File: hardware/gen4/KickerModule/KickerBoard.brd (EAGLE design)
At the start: 139.1 x 149.2 mm, 117 parts

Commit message: bit more work
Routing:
- net 3.3V: track 281.2 -> 507.0 mm, vias 8 -> 15
- net M1QB-3: track 0.00 -> 47.2 mm, vias 0 -> 1
- net SCK: track 106.7 -> 96.9 mm
- net MISO: track 98.2 -> 101.5 mm, vias 4 -> 6

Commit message: bit more work
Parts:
- added R22: 1k, SparkFun-Passives:0805
- added U$12: 13VZENER, rfc:THROUGH-HOLE-2
- moved PW_LED1 6.35 mm to (31.1, 94.6), flipped to the top, turned to 180 degrees
- moved CAP+_TEST 3.81 mm to (109.2, 134.0)
- moved R21 1.42 mm to (31.8, 89.5), turned to 270 degrees
- moved TMP 1.42 mm to (29.8, 89.5), turned to 90 degrees
- moved 3.3V_TEST 0.63 mm to (36.2, 94.6)
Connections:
- net 12V: now also U$12.-
- net 12VGND: now also U$12.+
- net 3.3V: now also R22.1
- net CHARGE_DONE: now also R22.2
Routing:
- net CHARGE_DONE: track 115.4 -> 150.0 mm
- net 12V: track 448.4 -> 475.8 mm
- net 3.3V: track 507.0 -> 523.8 mm, vias 15 -> 16
- net 12VGND: track 691.1 -> 700.0 mm
- net N$23: track 2.68 -> 11.0 mm, vias 0 -> 1
- net CAP+: track 190.0 -> 194.0 mm
- net GND: track 587.0 -> 585.0 mm

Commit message: new sizes + fixes
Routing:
- removed copper zone on layer 1, net 12VGND
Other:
- board size 139.1 x 149.2 mm -> 317.6 x 151.4 mm
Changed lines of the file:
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@@
 <setting verticaltext="up"/>
 </settings>
-<grid distance="0.635" unitdist="mm" unit="mil" style="lines" multiple="1" display="no" altdistance="0.3175" altunitdist="mm" altunit="mil"/>
+<grid distance="1" unitdist="mil" unit="mil" style="lines" multiple="1" display="no" altdistance="0.3175" altunitdist="mm" altunit="mil"/>
 <layers>
 <layer number="1" name="Top" color="4" fill="1" visible="yes" active="yes"/>
@@
 <wire x1="0" y1="20.955" x2="0" y2="119.365" width="0.4064" layer="20"/>
 <text x="-11.43" y="55.88" size="1.778" layer="20" rot="R90">MOTOR BOARD DIMENSION</text>
+<circle x="-156.54451875" y="29.649165625" radius="1.5875" width="0" layer="20"/>
+<circle x="-172.5444875" y="76.1492" radius="1.5875" width="0" layer="20"/>
+<circle x="-55.54471875" y="29.649165625" radius="1.5875" width="0" layer="20"/>
+<circle x="-156.54451875" y="128.149096875" radius="1.5875" width="0" layer="20"/>
+<circle x="-55.54471875" y="128.149096875" radius="1.5875" width="0" layer="20"/>
+<circle x="-39.544496875" y="76.1492" radius="1.5875" width="0" layer="20"/>
+<wire x1="-68.54469375" y1="7.649209375" x2="-33.544509375" y2="42.649140625" width="0" layer="20"/>
+<wire x1="-143.54454375" y1="7.649209375" x2="-68.54469375" y2="7.649209375" width="0" layer="20"/>
+<wire x1="-178.544475" y1="42.649140625" x2="-143.54454375" y2="7.649209375" width="0" layer="20"/>
+<wire x1="-178.544475" y1="112.649253125" x2="-178.544475" y2="42.649140625" width="0" layer="20"/>
+<wire x1="-141.044675" y1="150.14930625" x2="-178.544475" y2="112.649253125" width="0" layer="20"/>
+<wire x1="-71.0445625" y1="150.14930625" x2="-141.044675" y2="150.14930625" width="0" layer="20"/>
+<wire x1="-33.544509375" y1="112.649253125" x2="-71.0445625" y2="150.14930625" width="0" layer="20"/>
+<wire x1="-33.544509375" y1="42.649140625" x2="-33.544509375" y2="112.649253125" width="0" layer="20"/>
 </plain>
 <attributes>
@@
 <wire x1="28.575" y1="76.835" x2="22.225" y2="83.185" width="0.4064" layer="16"/>
 <wire x1="22.225" y1="83.185" x2="22.225" y2="83.82" width="0.4064" layer="16"/>
-<polygon width="0.254" layer="1" pour="cutout">
-<vertex x="0" y="-5.08"/>
-<vertex x="0.635" y="119.38"/>
-<vertex x="28.575" y="147.32"/>
-<vertex x="111.125" y="147.955"/>
-<vertex x="139.065" y="120.65"/>
-<vertex x="139.7" y="-5.08"/>
-</polygon>
 <polygon width="0.254" layer="16" pour="cutout">
 <vertex x="139.7" y="-5.08"/>

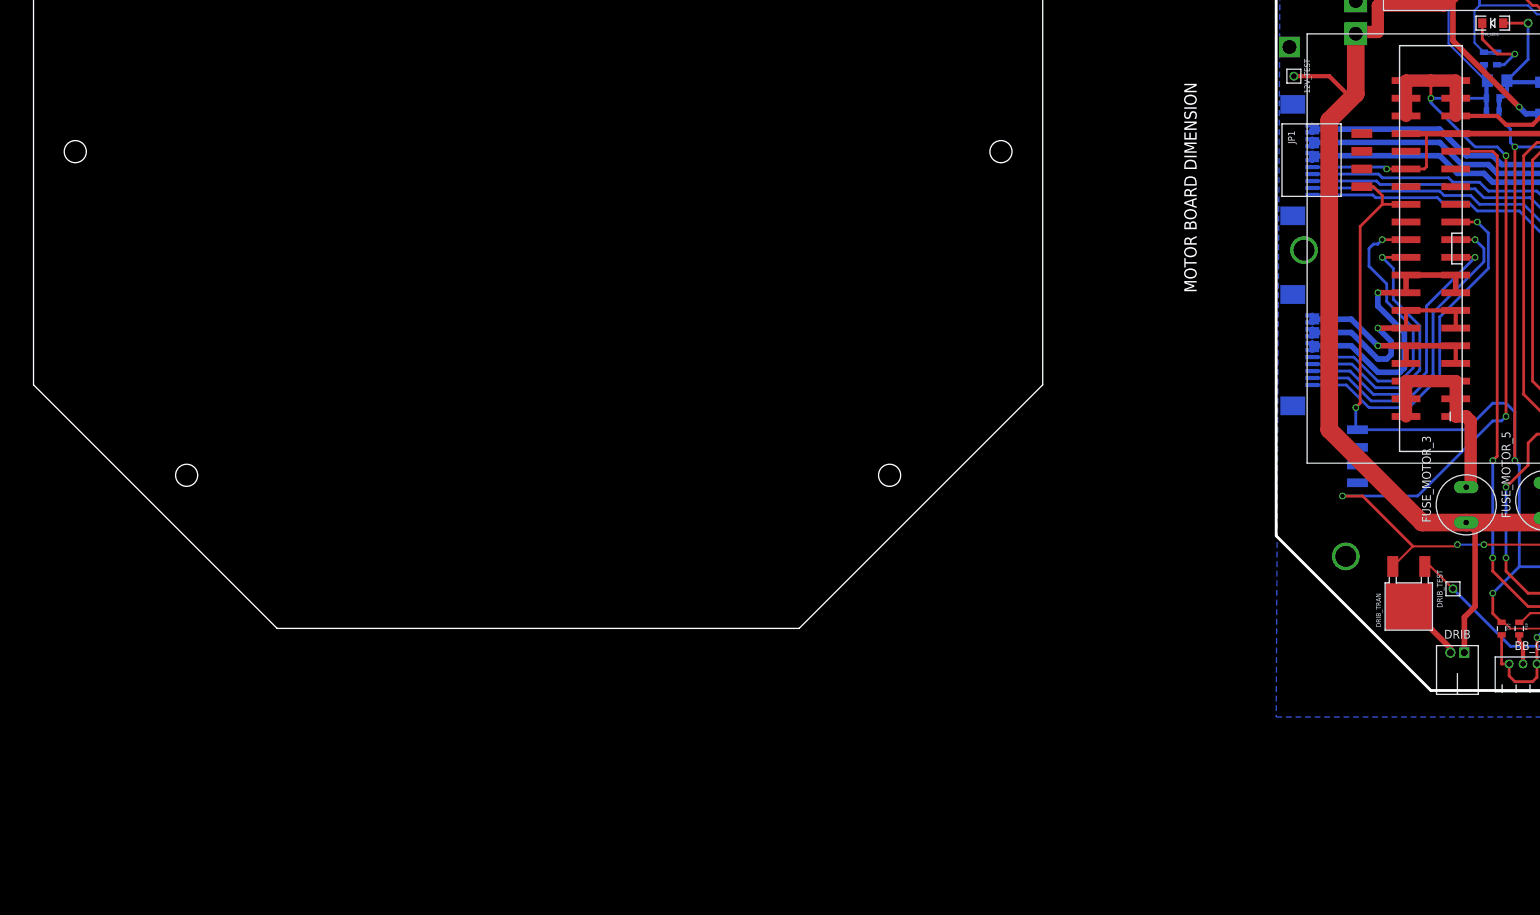
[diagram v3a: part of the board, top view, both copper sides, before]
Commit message: added ferrite bead on main board
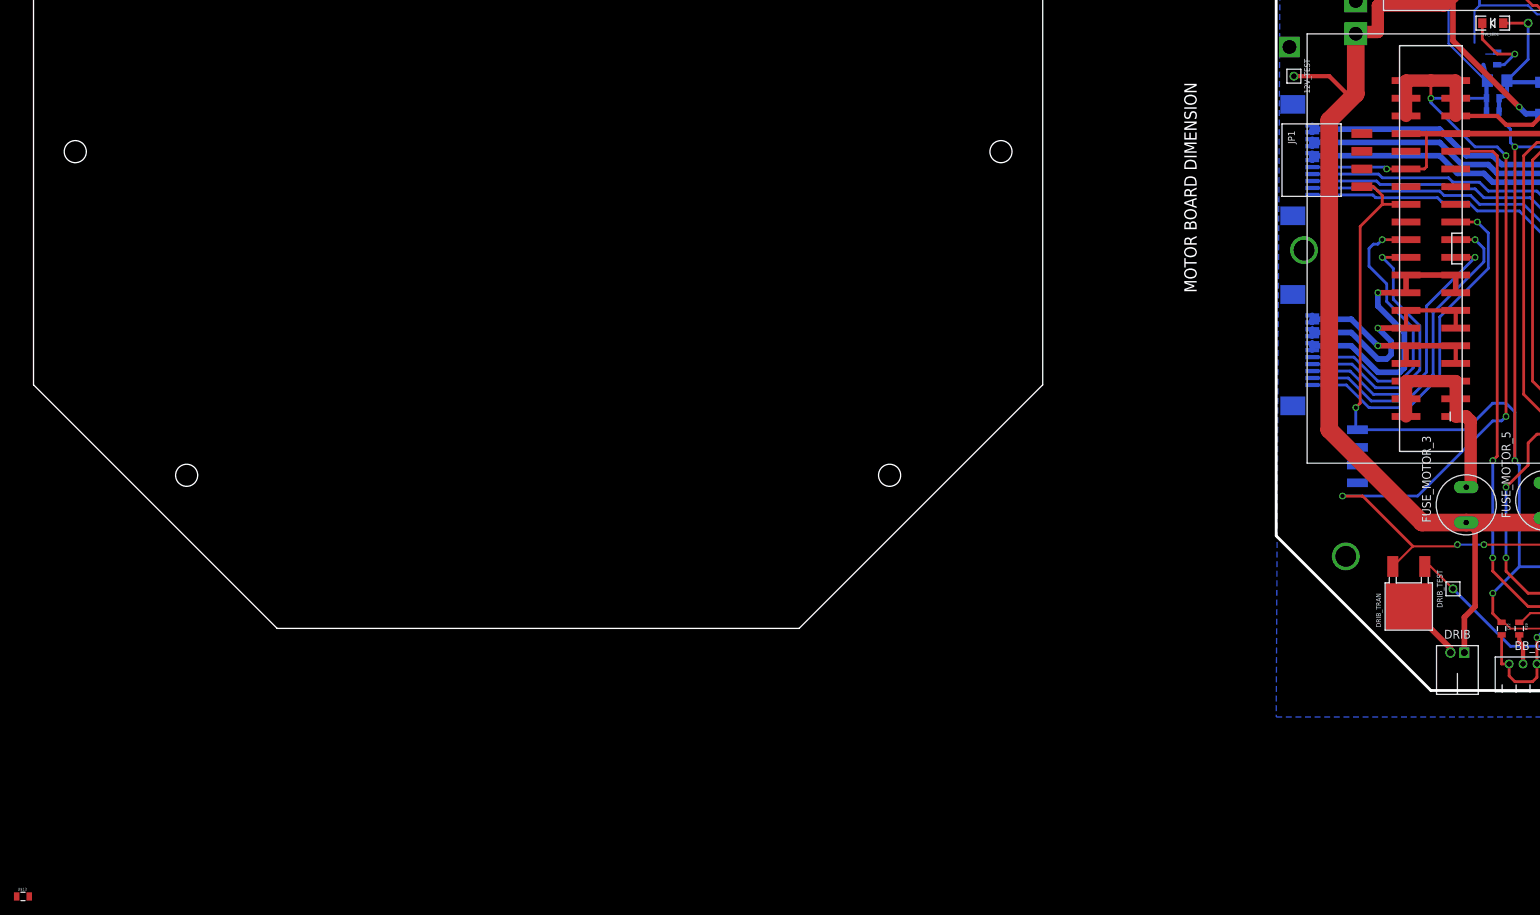
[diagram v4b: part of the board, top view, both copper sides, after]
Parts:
- removed TMP: 0, SparkFun-Passives:0805
- added U$13: INDUCTOR, gen3:0805
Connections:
- net 12VGND: now also U$13.1; no longer TMP.1
- net GND: now also U$13.2; no longer TMP.2
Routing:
- net GND: track 585.0 -> 580.8 mm
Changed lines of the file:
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@@
 <element name="RVOUT" library="SparkFun-Passives" package="0805" value="50.4k" x="57.785" y="107.95"/>
 <element name="SWITCH_Q" library="gen3" package="DPAK" value="" x="69.215" y="107.95" rot="R270"/>
-<element name="TMP" library="SparkFun-Passives" package="0805" value="0" x="29.845" y="89.535" rot="MR90"/>
 <element name="U$1" library="kickerchips" package="SOT23-5" value="FAN31111" x="112.395" y="104.775" rot="R270"/>
 <element name="U$3" library="gen3" package="10-TRANSFORMER" value="32052-TRANSFORMER" x="18.415" y="114.935"/>
@@
 <element name="R22" library="SparkFun-Passives" package="0805" value="1k" x="46.355" y="22.86"/>
 <element name="U$12" library="rfc" package="THROUGH-HOLE-2" value="13VZENER" x="123.825" y="131.445" rot="R135"/>
+<element name="U$13" library="gen3" package="0805" value="INDUCTOR" x="-180.0606" y="-30.861"/>
 </elements>
 <signals>
@@
 <contactref element="R18" pad="1"/>
 <contactref element="BATCLAMP2" pad="A"/>
-<contactref element="TMP" pad="2"/>
 <contactref element="BB_CON" pad="5"/>
 <contactref element="C12" pad="2"/>
@@
 <via x="102.87" y="102.235" extent="1-16" drill="0.6"/>
 <wire x1="102.87" y1="102.235" x2="97.79" y2="107.315" width="0.3048" layer="16"/>
-<wire x1="31.75" y1="90.435" x2="29.845" y2="90.435" width="0.3048" layer="16"/>
 <wire x1="33.465" y1="2.54" x2="32.385" y2="2.54" width="0.4064" layer="1"/>
 <wire x1="32.385" y1="2.54" x2="32.385" y2="6.72" width="0.4064" layer="1"/>
@@
 <wire x1="49.53" y1="82.8675" x2="49.53" y2="81.915" width="0.4064" layer="1"/>
 <wire x1="49.53" y1="81.915" x2="48.895" y2="81.28" width="0.4064" layer="1"/>
-<wire x1="29.845" y1="90.435" x2="30.11" y2="90.17" width="0" layer="16"/>
 <wire x1="30.11" y1="90.17" x2="31.75" y2="90.17" width="0" layer="16"/>
 <wire x1="31.75" y1="90.17" x2="31.75" y2="90.435" width="0" layer="16"/>
@@
 <via x="126.365" y="62.865" extent="1-16" drill="0.6"/>
 <wire x1="126.365" y1="62.865" x2="122.7963" y2="62.865" width="0.4064" layer="1"/>
-<wire x1="28.495" y1="91.785" x2="29.845" y2="90.435" width="0.3048" layer="16"/>
+<contactref element="U$13" pad="2"/>
 <wire x1="129.9337" y1="78.105" x2="127.395" y2="92.075" width="0" layer="19" extent="1-16"/>
 <wire x1="61.105" y1="115.57" x2="60.96" y2="115.57" width="0" layer="19" extent="16-16"/>
+<wire x1="30.11" y1="90.17" x2="28.495" y2="91.785" width="0" layer="19" extent="16-16"/>
 <wire x1="12.305" y1="76.2" x2="15.605" y2="73.93" width="0" layer="19" extent="1-16"/>
 <wire x1="122.7963" y1="73.025" x2="122.7963" y2="78.105" width="0" layer="19" extent="1-1"/>
@@
 <wire x1="11.67" y1="31.115" x2="14.605" y2="43.18" width="0" layer="19" extent="16-16"/>
 <wire x1="127.395" y1="34.29" x2="129.4925" y2="49.26" width="0" layer="19" extent="16-16"/>
+<wire x1="-179.1606" y1="-30.861" x2="5.175" y2="46.625" width="0" layer="19" extent="1-16"/>
 </signal>
 <signal name="3.3V">
@@
 <contactref element="C11" pad="2"/>
 <contactref element="3.3REG1" pad="DRAIN"/>
-<contactref element="TMP" pad="1"/>
 <contactref element="DRIB_TRAN" pad="SOURCE"/>
 <contactref element="MOTOR1" pad="38"/>
@@
 <contactref element="MOTOR1" pad="39"/>
 <contactref element="MOTOR1" pad="37"/>
-<wire x1="29.845" y1="88.635" x2="29.7675" y2="88.635" width="0.6096" layer="16"/>
 <wire x1="29.7675" y1="88.635" x2="30.35" y2="86.36" width="0.6096" layer="16"/>
 <wire x1="30.215" y1="81.915" x2="30.215" y2="83.82" width="0.6096" layer="16"/>
@@
 <wire x1="117.475" y1="124.46" x2="123.825" y2="130.81" width="0.508" layer="1"/>
 <wire x1="123.825" y1="130.81" x2="123.825" y2="131.445" width="0.508" layer="1"/>
+<contactref element="U$13" pad="1"/>
+<wire x1="9.525" y1="26.67" x2="-180.9606" y2="-30.861" width="0" layer="19" extent="1-1"/>
 </signal>
 <signal name="COMP_OUT">

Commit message: added ferrite beads
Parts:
- moved U$13 256.9 mm to (31.3, 115.3), flipped to the bottom, turned to 270 degrees
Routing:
- net GND: track 580.8 -> 588.0 mm, vias 22 -> 23
- net 12VGND: track 699.9 -> 704.1 mm
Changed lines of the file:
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@@
 <element name="R22" library="SparkFun-Passives" package="0805" value="1k" x="46.355" y="22.86"/>
 <element name="U$12" library="rfc" package="THROUGH-HOLE-2" value="13VZENER" x="123.825" y="131.445" rot="R135"/>
-<element name="U$13" library="gen3" package="0805" value="INDUCTOR" x="-180.0606" y="-30.861"/>
+<element name="U$13" library="gen3" package="0805" value="INDUCTOR" x="31.2928" y="115.2652" rot="MR270"/>
 </elements>
 <signals>
@@
 <wire x1="11.67" y1="31.115" x2="14.605" y2="43.18" width="0" layer="19" extent="16-16"/>
 <wire x1="127.395" y1="34.29" x2="129.4925" y2="49.26" width="0" layer="19" extent="16-16"/>
-<wire x1="-179.1606" y1="-30.861" x2="5.175" y2="46.625" width="0" layer="19" extent="1-16"/>
+<wire x1="36.195" y1="111.125" x2="32.9946" y2="111.125" width="0.1778" layer="1"/>
+<wire x1="32.9946" y1="111.125" x2="31.3944" y2="112.7252" width="0.1778" layer="1"/>
+<via x="31.3944" y="112.7252" extent="1-16" drill="0.4064"/>
+<wire x1="31.3944" y1="112.7252" x2="31.3944" y2="114.2636" width="0.1778" layer="16"/>
+<wire x1="31.3944" y1="114.2636" x2="31.2928" y2="114.3652" width="0.1778" layer="16"/>
 </signal>
 <signal name="3.3V">
@@
 <wire x1="123.825" y1="130.81" x2="123.825" y2="131.445" width="0.508" layer="1"/>
 <contactref element="U$13" pad="1"/>
-<wire x1="9.525" y1="26.67" x2="-180.9606" y2="-30.861" width="0" layer="19" extent="1-1"/>
+<wire x1="34.925" y1="114.935" x2="33.6948" y2="116.1652" width="0.1778" layer="16"/>
+<wire x1="33.6948" y1="116.1652" x2="31.2928" y2="116.1652" width="0.1778" layer="16"/>
 </signal>
 <signal name="COMP_OUT">

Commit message: main board routing finished
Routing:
- net GND: track 588.0 -> 808.5 mm, vias 23 -> 31
- net MISO: track 101.5 -> 231.0 mm, vias 6 -> 11
- net MOSI: track 82.7 -> 209.8 mm, vias 2 -> 9
- net SCK: track 96.9 -> 215.3 mm, vias 4 -> 8
- net M1QB-4: track 0.00 -> 91.5 mm, vias 0 -> 5
- net M1QB-1: track 0.00 -> 65.0 mm, vias 0 -> 1
- net M1QA-2: track 0.00 -> 59.2 mm, vias 0 -> 4
- net M1QA-1: track 0.00 -> 52.6 mm, vias 0 -> 1
- net M1QA-4: track 0.00 -> 47.7 mm, vias 0 -> 1
- net M1QA-3: track 0.00 -> 46.1 mm, vias 0 -> 1
- net M1QB-2: track 0.00 -> 43.2 mm, vias 0 -> 2
- net 12VGND: track 704.1 -> 702.7 mm
- net SS4: track 129.6 -> 130.3 mm

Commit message: new shape
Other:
- board size 317.6 x 151.4 mm -> 513.1 x 154.5 mm
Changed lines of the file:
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@@
 <wire x1="-33.544509375" y1="112.649253125" x2="-71.0445625" y2="150.14930625" width="0" layer="20"/>
 <wire x1="-33.544509375" y1="42.649140625" x2="-33.544509375" y2="112.649253125" width="0" layer="20"/>
+<circle x="324.508875" y="64.897" radius="1.5875" width="0" layer="20"/>
+<circle x="184.508903125" y="64.897" radius="1.5875" width="0" layer="20"/>
+<circle x="219.50883125" y="125.518671875" radius="1.5875" width="0" layer="20"/>
+<circle x="289.508690625" y="125.518671875" radius="1.5875" width="0" layer="20"/>
+<circle x="308.131971875" y="19.901915625" radius="1.5875" width="0" layer="20"/>
+<circle x="200.88580625" y="19.901915625" radius="1.5875" width="0" layer="20"/>
+<wire x1="294.50868125" y1="-4.38505625" x2="214.508840625" y2="-4.38505625" width="0" layer="20"/>
+<wire x1="294.50868125" y1="-4.38505625" x2="214.508840625" y2="-4.38505625" width="0" layer="20" curve="300.000116"/>
 </plain>
 <attributes>

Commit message: new shape part2
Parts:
- moved DRIB 13.3 mm to (26.0, 16.5)
- moved DRIB_TRAN 10.3 mm to (21.0, 21.0), flipped to the bottom
- moved BB_CON 8.28 mm to (38.1, 10.8)
- moved R25 8.25 mm to (41.3, 141.6)
- moved R13 6.99 mm to (37.5, 142.2)
- moved R16 6.99 mm to (37.5, 140.3)
- moved R3 6.99 mm to (37.5, 138.4)
- moved U$6 6.98 mm to (41.3, 146.1)
- moved DRIB_TEST 6.35 mm to (30.5, 9.53)
- moved C12 6.02 mm to (34.3, 13.3), flipped to the bottom
- moved R19 6.02 mm to (36.8, 13.3), flipped to the bottom
- moved R20 5.72 mm to (41.3, 13.3), flipped to the bottom
- moved CHARGE_D 4.44 mm to (18.4, 121.9)
- moved U$2 3.86 mm to (43.8, 131.4)
- moved U$7 3.18 mm to (16.5, 128.9)
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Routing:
- net SS1: track 121.2 -> 0.00 mm, vias 2 -> 0
- net BB_OUT: track 75.5 -> 0.00 mm, vias 2 -> 0
- net BB_IN: track 70.0 -> 0.00 mm
- net DRIB: track 69.6 -> 0.00 mm, vias 1 -> 0
- net GND: track 808.5 -> 755.3 mm, vias 31 -> 29
- net 3.3V: track 524.2 -> 504.4 mm, vias 16 -> 15
- net 12VGND: track 702.7 -> 684.0 mm
- net 12V: track 475.8 -> 461.3 mm
- net TO_DRIB: track 9.10 -> 0.00 mm
- net DIVCAP: track 121.7 -> 116.4 mm
- net TRANS_OUT: track 9.38 -> 4.94 mm
- net N$32: track 4.40 -> 0.00 mm
- net N$40: track 4.26 -> 0.00 mm
- net N$36: track 9.75 -> 13.9 mm
- net N$29: track 26.7 -> 29.2 mm
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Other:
- board size 513.1 x 154.5 mm -> 328.9 x 149.3 mm
